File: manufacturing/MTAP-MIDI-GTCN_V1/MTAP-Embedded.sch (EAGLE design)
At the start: 15 parts, among them IC1 ESP32-WROOM-32D, IC2 AMS1117-3.3, X1 USB4140-GF-0230-C

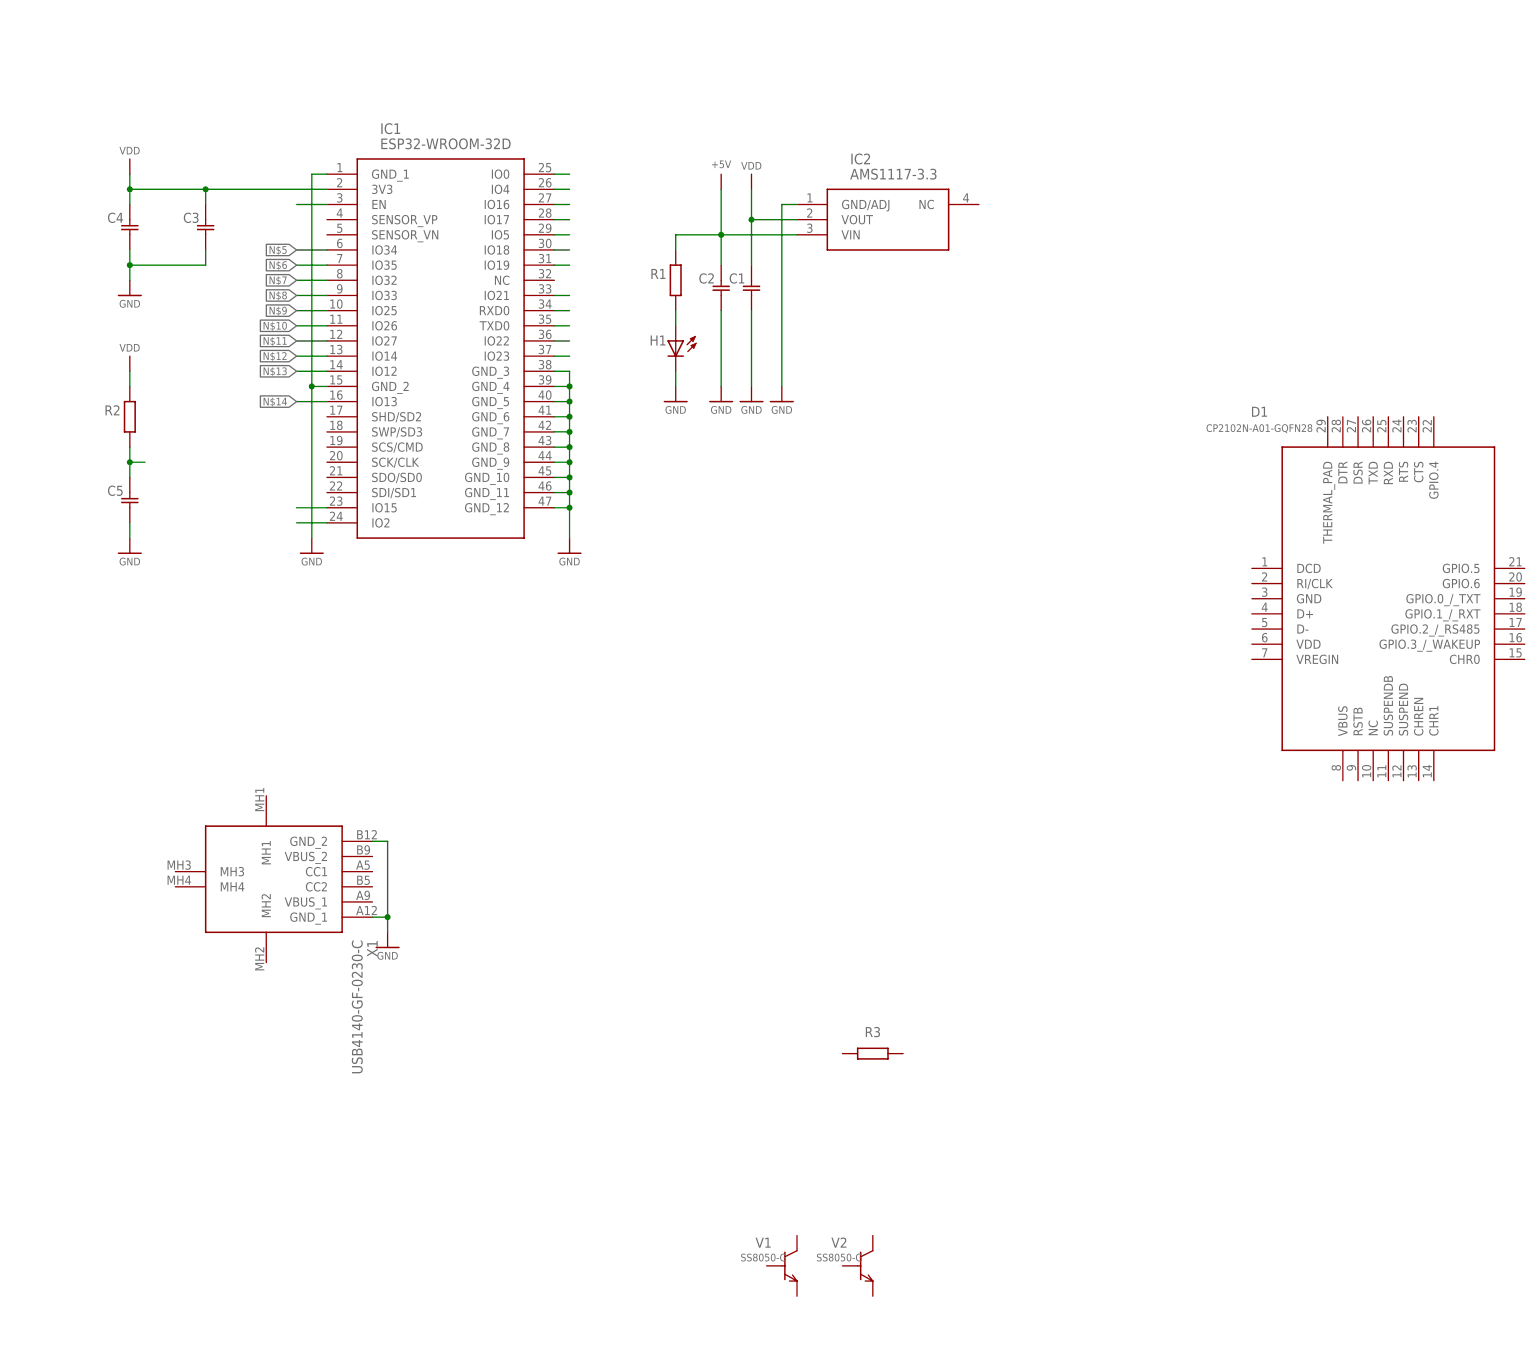
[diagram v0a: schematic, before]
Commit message: added Logo and tested ESP footprints
schematic for ESP complete
except values
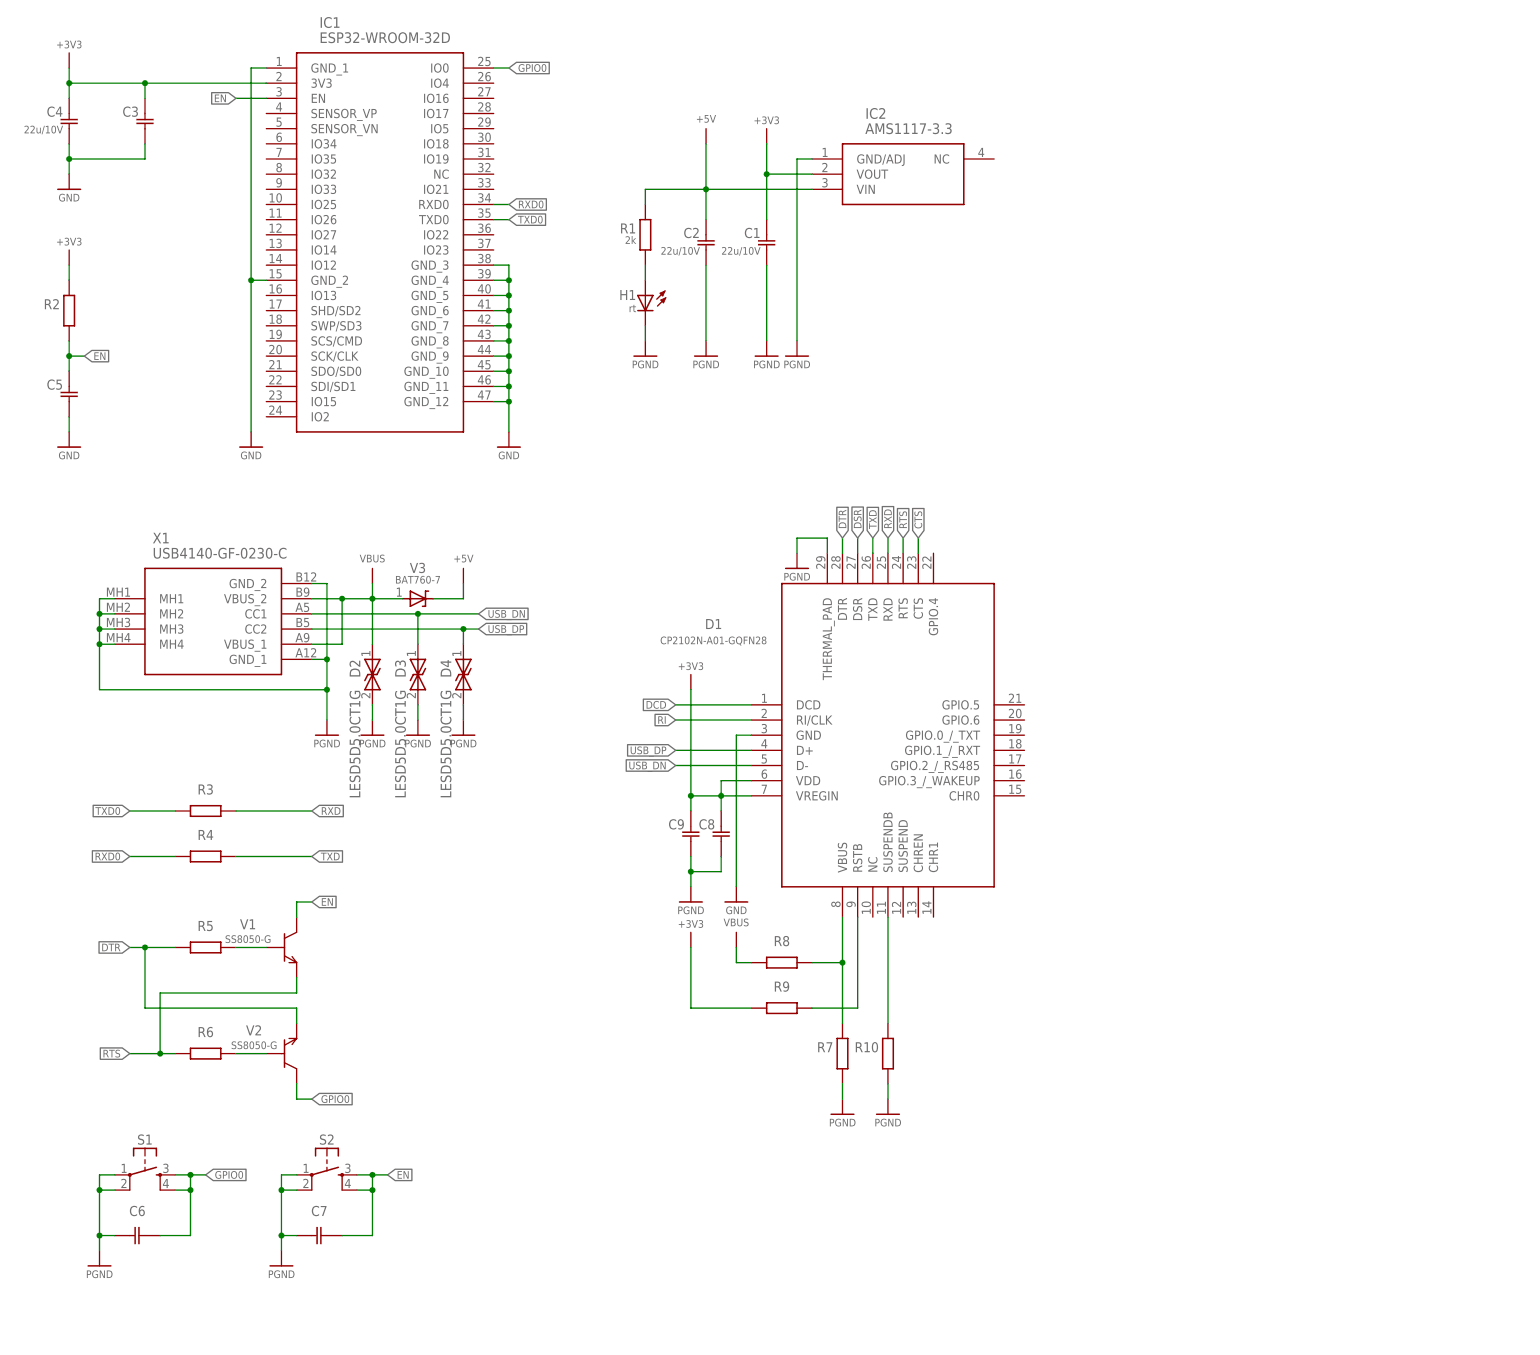
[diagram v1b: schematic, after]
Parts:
- added C6, C7: (no value), rcl_GruS:C-EULC0805
- added C8, C9: (no value), rcl_GruS:C-EUC0805
- added D2, D3, D4: LESD5D5.0CT1G, diode_GruS:LESD5D5.0CT1G
- added R10, R7: (no value), rcl_GruS:R-EUSR0805
- added R4, R5, R6, R8, R9: (no value), rcl_GruS:R-EU_R0805
- added S1, S2: (no value), switch_GruS:TASTE10XXSMD
- added V3: BAT760-7, diode_GruS:BAT760-7
- C1, C2, C4: value (none) -> 22u/10V
- H1: value (none) -> rt
- R1: value (none) -> 2k
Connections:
- removed net N$10: IC1.IO26
- removed net N$11: IC1.IO27
- removed net N$12: IC1.IO14
- removed net N$13: IC1.IO12
- removed net N$14: IC1.IO13
- removed net N$21: IC1.IO15
- removed net N$22: IC1.IO2
- removed net N$23: IC1.IO0
- removed net N$24: IC1.IO4
- removed net N$25: IC1.IO16
- removed net N$26: IC1.IO17
- removed net N$27: IC1.IO5
- removed net N$28: IC1.IO18
- removed net N$29: IC1.IO19
- removed net N$30: IC1.IO21
- removed net N$31: IC1.RXD0
- removed net N$32: IC1.TXD0
- removed net N$33: IC1.IO22
- removed net N$34: IC1.IO23
- removed net N$35: C5.1, R2.1
- removed net N$5: IC1.IO34
- removed net N$6: IC1.IO35
- removed net N$7: IC1.IO32
- removed net N$8: IC1.IO33
- removed net N$9: IC1.IO25
- removed net VDD: C1.1, C3.1, C4.1, IC1.3V3, IC2.VOUT, R2.2
- new net +3V3: C1.1, C3.1, C4.1, C8.1, C9.1, D1.VDD, D1.VREGIN, IC1.3V3, IC2.VOUT, R2.2, R9.1
- new net CTS: D1.CTS
- new net DCD: D1.DCD
- new net DSR: D1.DSR
- new net DTR: D1.DTR, R5.1, V2.E
- new net EN: C5.1, C7.1, IC1.EN, R2.1, S2.S, S2.S1, V1.C
- new net GPIO0: C6.1, IC1.IO0, S1.S, S1.S1, V2.C
- new net N$15: R5.2, V1.B
- new net N$16: R6.2, V2.B
- new net N$3: D1.SUSPENDB, R10.2
- new net N$4: D1.RSTB, R9.2
- new net PGND: C1.2, C2.2, C6.2, C7.2, C8.2, C9.2, D1.THERMAL_PAD, D2.2, D3.2, D4.2, H1.C, IC2.GND/ADJ, R10.1, R7.1, S1.P, S1.P1, S2.P, S2.P1, X1.GND_1, X1.GND_2, X1.MH1, X1.MH2, X1.MH3, X1.MH4
- new net RI: D1.RI/CLK
- new net RTS: D1.RTS, R6.1, V1.E
- new net RXD: D1.RXD, R3.2
- new net RXD0: IC1.RXD0, R4.1
- new net TXD: D1.TXD, R4.2
- new net TXD0: IC1.TXD0, R3.1
- new net USB_DN: D1.D-, D3.1, X1.CC1
- new net USB_DP: D1.D+, D4.1, X1.CC2
- new net VBUS: D2.1, R8.1, V3.K, X1.VBUS_1, X1.VBUS_2
- net +5V: now also V3.A
- net GND: now also D1.GND; no longer C1.2, C2.2, H1.C, IC2.GND/ADJ, X1.GND_1, X1.GND_2
- net N$2: now also D1.VBUS, R7.2, R8.2; no longer IC1.EN
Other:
- moved on the sheet: C1, C2, C3, C4, C5, D1, H1, IC1, IC2, R1, R2, R3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

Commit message: upd Embedded
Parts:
- added R11: 0R, rcl_GruS:R-EU_R0805
- IC1: value ESP32-WROOM-32D -> ESP32-WROOM-32UE-N8; device modul_GruS:ESP32-WROOM-32D -> modul_GruS:ESP32-WROOM-32UE-N8
- R7: value (none) -> 47k5
- R8: value (none) -> 22k1
- S1, S2: device switch_GruS:TASTE10XXSMD -> switch_GruS:TASTE10XXWE
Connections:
- net GND: now also R11.2
- net PGND: now also R11.1
- net USB_DN: now also D4.1, X1.CC2; no longer D3.1, X1.CC1
- net USB_DP: now also D3.1, X1.CC1; no longer D4.1, X1.CC2
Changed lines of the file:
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@@
 </variantdefs>
 <classes>
-<class number="0" name="default" width="0" drill="0">
+<class number="0" name="default" width="0.254" drill="0">
+</class>
+<class number="1" name="+3V3" width="0.8128" drill="0">
+</class>
+<class number="2" name="VBUS" width="0.8128" drill="0">
+</class>
+<class number="3" name="+5V" width="0.8128" drill="0">
 </class>
 </classes>
 <parts>
 <part name="FRAMES1" library="frames_GruS" library_urn="urn:adsk.eagle:library:27468648" deviceset="HTL-A4H-V1" device=""/>
-<part name="IC1" library="modul_GruS" library_urn="urn:adsk.eagle:library:13580331" deviceset="ESP32-WROOM-32D" device="" package3d_urn="urn:adsk.eagle:package:37740908/1"/>
+<part name="IC1" library="modul_GruS" library_urn="urn:adsk.eagle:library:13580331" deviceset="ESP32-WROOM-32UE-N8" device="" package3d_urn="urn:adsk.eagle:package:37940893/1"/>
 <part name="IC2" library="vreg_GruS" library_urn="urn:adsk.eagle:library:13581047" deviceset="AMS1117-3.3" device="" package3d_urn="urn:adsk.eagle:package:37738375/1"/>
 <part name="C1" library="rcl_GruS" library_urn="urn:adsk.eagle:library:13572313" deviceset="C-EU" device="C0805" package3d_urn="urn:adsk.eagle:package:23617/2" value="22u/10V"/>
@@
 <part name="V2" library="transistor_GruS" library_urn="urn:adsk.eagle:library:13581291" deviceset="SS8050-G" device="" package3d_urn="urn:adsk.eagle:package:37738390/1"/>
 <part name="D1" library="ic_GruS" library_urn="urn:adsk.eagle:library:13571010" deviceset="CP2102N-A01-GQFN28" device="" package3d_urn="urn:adsk.eagle:package:37738757/2"/>
-<part name="X1" library="con_GruS" library_urn="urn:adsk.eagle:library:13569504" deviceset="USB4140-GF-0230-C" device="" package3d_urn="urn:adsk.eagle:package:37738890/1"/>
+<part name="X1" library="con_GruS" library_urn="urn:adsk.eagle:library:13569504" deviceset="USB4140-GF-0230-C" device="" package3d_urn="urn:adsk.eagle:package:37738890/2"/>
 <part name="D2" library="diode_GruS" library_urn="urn:adsk.eagle:library:13569696" deviceset="LESD5D5.0CT1G" device="" package3d_urn="urn:adsk.eagle:package:37738879/1"/>
 <part name="D3" library="diode_GruS" library_urn="urn:adsk.eagle:library:13569696" deviceset="LESD5D5.0CT1G" device="" package3d_urn="urn:adsk.eagle:package:37738879/1"/>
@@
 <part name="R6" library="rcl_GruS" library_urn="urn:adsk.eagle:library:13572313" deviceset="R-EU_" device="R0805" package3d_urn="urn:adsk.eagle:package:18365371/1"/>
 <part name="VBUS1" library="supply_GruS" library_urn="urn:adsk.eagle:library:13579815" deviceset="VBUS" device=""/>
-<part name="S1" library="switch_GruS" library_urn="urn:adsk.eagle:library:13571161" deviceset="TASTE10XX" device="SMD" package3d_urn="urn:adsk.eagle:package:18368075/2"/>
+<part name="S1" library="switch_GruS" library_urn="urn:adsk.eagle:library:13571161" deviceset="TASTE10XX" device="WE" package3d_urn="urn:adsk.eagle:package:18368072/1"/>
 <part name="C6" library="rcl_GruS" library_urn="urn:adsk.eagle:library:13572313" deviceset="C-EUL" device="C0805" package3d_urn="urn:adsk.eagle:package:23617/2"/>
-<part name="S2" library="switch_GruS" library_urn="urn:adsk.eagle:library:13571161" deviceset="TASTE10XX" device="SMD" package3d_urn="urn:adsk.eagle:package:18368075/2"/>
+<part name="S2" library="switch_GruS" library_urn="urn:adsk.eagle:library:13571161" deviceset="TASTE10XX" device="WE" package3d_urn="urn:adsk.eagle:package:18368072/1"/>
 <part name="C7" library="rcl_GruS" library_urn="urn:adsk.eagle:library:13572313" deviceset="C-EUL" device="C0805" package3d_urn="urn:adsk.eagle:package:23617/2"/>
 <part name="+3V1" library="supply_GruS" library_urn="urn:adsk.eagle:library:13579815" deviceset="+3V3" device=""/>
@@
 <part name="R9" library="rcl_GruS" library_urn="urn:adsk.eagle:library:13572313" deviceset="R-EU_" device="R0805" package3d_urn="urn:adsk.eagle:package:18365371/1"/>
 <part name="+3V2" library="supply_GruS" library_urn="urn:adsk.eagle:library:13579815" deviceset="+3V3" device=""/>
-<part name="R7" library="rcl_GruS" library_urn="urn:adsk.eagle:library:13572313" deviceset="R-EUS" device="R0805" package3d_urn="urn:adsk.eagle:package:18365371/1"/>
-<part name="R8" library="rcl_GruS" library_urn="urn:adsk.eagle:library:13572313" deviceset="R-EU_" device="R0805" package3d_urn="urn:adsk.eagle:package:18365371/1"/>
+<part name="R7" library="rcl_GruS" library_urn="urn:adsk.eagle:library:13572313" deviceset="R-EUS" device="R0805" package3d_urn="urn:adsk.eagle:package:18365371/1" value="47k5"/>
+<part name="R8" library="rcl_GruS" library_urn="urn:adsk.eagle:library:13572313" deviceset="R-EU_" device="R0805" package3d_urn="urn:adsk.eagle:package:18365371/1" value="22k1"/>
 <part name="+3V3" library="supply_GruS" library_urn="urn:adsk.eagle:library:13579815" deviceset="+3V3" device=""/>
 <part name="+3V4" library="supply_GruS" library_urn="urn:adsk.eagle:library:13579815" deviceset="+3V3" device=""/>
@@
 <part name="PGND14" library="supply_GruS" library_urn="urn:adsk.eagle:library:13579815" deviceset="PGND" device=""/>
 <part name="PGND15" library="supply_GruS" library_urn="urn:adsk.eagle:library:13579815" deviceset="PGND" device=""/>
+<part name="R11" library="rcl_GruS" library_urn="urn:adsk.eagle:library:13572313" deviceset="R-EU_" device="R0805" package3d_urn="urn:adsk.eagle:package:18365371/1" value="0R"/>
+<part name="PGND13" library="supply_GruS" library_urn="urn:adsk.eagle:library:13579815" deviceset="PGND" device=""/>
+<part name="GND2" library="supply_GruS" library_urn="urn:adsk.eagle:library:13579815" deviceset="GND" device=""/>
 </parts>
 <sheets>
@@
 <instance part="PGND15" gate="G$1" x="142.24" y="83.82" smashed="yes">
 <attribute name="VALUE" x="142.24" y="81.788" size="1.27" layer="96" font="vector" align="bottom-center"/>
+</instance>
+<instance part="R11" gate="G$1" x="106.68" y="86.36" smashed="yes">
+<attribute name="NAME" x="106.68" y="89.1286" size="1.6764" layer="95" font="vector" align="bottom-center"/>
+<attribute name="VALUE" x="106.68" y="87.63" size="1.27" layer="96" font="vector" align="bottom-center"/>
+</instance>
+<instance part="PGND13" gate="G$1" x="99.06" y="81.28" smashed="yes">
+<attribute name="VALUE" x="99.06" y="79.248" size="1.27" layer="96" font="vector" align="bottom-center"/>
+</instance>
+<instance part="GND2" gate="1" x="114.3" y="81.28" smashed="yes">
+<attribute name="VALUE" x="114.3" y="79.248" size="1.27" layer="96" font="vector" align="bottom-center"/>
 </instance>
 </instances>
@@
 <pinref part="GND1" gate="1" pin="GND"/>
 </segment>
+<segment>
+<pinref part="R11" gate="G$1" pin="2"/>
+<wire x1="111.76" y1="86.36" x2="114.3" y2="86.36" width="0.1524" layer="91"/>
+<wire x1="114.3" y1="86.36" x2="114.3" y2="83.82" width="0.1524" layer="91"/>
+<pinref part="GND2" gate="1" pin="GND"/>
+</segment>
 </net>
 <net name="N$1" class="0">
@@
 <net name="USB_DP" class="0">
 <segment>
+<pinref part="D1" gate="G$1" pin="D+"/>
+<wire x1="127" y1="144.78" x2="114.3" y2="144.78" width="0.1524" layer="91"/>
+<label x="114.3" y="144.78" size="1.27" layer="95" rot="R180" xref="yes"/>
+</segment>
+<segment>
+<pinref part="X1" gate="G$1" pin="CC1"/>
+<wire x1="53.34" y1="167.64" x2="71.12" y2="167.64" width="0.1524" layer="91"/>
+<pinref part="D3" gate="G$1" pin="1"/>
+<wire x1="71.12" y1="167.64" x2="81.28" y2="167.64" width="0.1524" layer="91"/>
+<wire x1="71.12" y1="162.56" x2="71.12" y2="167.64" width="0.1524" layer="91"/>
+<junction x="71.12" y="167.64"/>
+<label x="81.28" y="167.64" size="1.27" layer="95" xref="yes"/>
+</segment>
+</net>
+<net name="USB_DN" class="0">
+<segment>
+<pinref part="D1" gate="G$1" pin="D-"/>
+<wire x1="127" y1="142.24" x2="114.3" y2="142.24" width="0.1524" layer="91"/>
+<label x="114.3" y="142.24" size="1.27" layer="95" rot="R180" xref="yes"/>
+</segment>
+<segment>
 <pinref part="X1" gate="G$1" pin="CC2"/>
 <wire x1="53.34" y1="165.1" x2="78.74" y2="165.1" width="0.1524" layer="91"/>
@@
 <wire x1="78.74" y1="162.56" x2="78.74" y2="165.1" width="0.1524" layer="91"/>
 <junction x="78.74" y="165.1"/>
-</segment>
-<segment>
-<pinref part="D1" gate="G$1" pin="D+"/>
-<wire x1="127" y1="144.78" x2="114.3" y2="144.78" width="0.1524" layer="91"/>
-<label x="114.3" y="144.78" size="1.27" layer="95" rot="R180" xref="yes"/>
-</segment>
-</net>
-<net name="USB_DN" class="0">
-<segment>
-<pinref part="X1" gate="G$1" pin="CC1"/>
-<wire x1="53.34" y1="167.64" x2="71.12" y2="167.64" width="0.1524" layer="91"/>
-<pinref part="D3" gate="G$1" pin="1"/>
-<wire x1="71.12" y1="167.64" x2="81.28" y2="167.64" width="0.1524" layer="91"/>
-<wire x1="71.12" y1="162.56" x2="71.12" y2="167.64" width="0.1524" layer="91"/>
-<junction x="71.12" y="167.64"/>
-<label x="81.28" y="167.64" size="1.27" layer="95" xref="yes"/>
-</segment>
-<segment>
-<pinref part="D1" gate="G$1" pin="D-"/>
-<wire x1="127" y1="142.24" x2="114.3" y2="142.24" width="0.1524" layer="91"/>
-<label x="114.3" y="142.24" size="1.27" layer="95" rot="R180" xref="yes"/>
 </segment>
 </net>
@@
 <pinref part="R7" gate="G$1" pin="1"/>
 </segment>
-</net>
+<segment>
+<pinref part="R11" gate="G$1" pin="1"/>
+<wire x1="101.6" y1="86.36" x2="99.06" y2="86.36" width="0.1524" layer="91"/>
+<wire x1="99.06" y1="86.36" x2="99.06" y2="83.82" width="0.1524" layer="91"/>
+<pinref part="PGND13" gate="G$1" pin="PGND"/>
+</segment>
+</net>

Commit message: Update Embedded
added PCM ADC to PCB
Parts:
- added C10, C12: 1u, rcl_GruS:C-EUC0805
- added C11, C13, C14: 10u, rcl_GruS:C-EUC0805
- added C15, C17, C18, C20: 100n, rcl_GruS:C-EUC0805
- added IC3: PCM1821IRTER, adc-dac_GruS:PCM1821IRTER
- added X2: (no value), con_GruS:JUMPSMD1FACH-1SHORT
- C3, C5: value (none) -> 100n/50V
- C6, C7: value (none) -> 100n
- R10, R2, R5, R6: value (none) -> 10k
- R11: device rcl_GruS:R-EU_R0805 -> con_GruS:JUMPSMD1FACH-1SHORT
- R3, R4: value (none) -> 0R
- R9: value (none) -> 2k
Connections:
- new net AVDD: C12.1, C18.1, IC3.AVDD, X2.2
- new net BCLK: IC1.IO22, IC3.BCLK
- new net FSYNC: IC1.IO23, IC3.FSYNC
- new net FTM0: IC3.FMT0
- new net GPIO12: IC1.IO12
- new net GPIO13: IC1.IO13
- new net GPIO14: IC1.IO14
- new net GPIO15: IC1.IO15
- new net GPIO16: IC1.IO16
- new net GPIO17: IC1.IO17
- new net GPIO2: IC1.IO2
- new net GPIO25: IC1.IO25
- new net GPIO26: IC1.IO26
- new net GPIO27: IC1.IO27
- new net GPIO32: IC1.IO32
- new net GPIO33: IC1.IO33
- new net GPIO34: IC1.IO34
- new net GPIO35: IC1.IO35
- new net GPIO4: IC1.IO4
- new net IN1M: IC3.IN1M
- new net IN1P: IC3.IN1P
- new net IN2M: IC3.IN2M
- new net IN2P: IC3.IN2P
- new net MD0: IC1.IO18, IC3.MD0
- new net MD1: IC1.IO19, IC3.MD1
- new net MSZ: IC1.IO5, IC3.MSZ
- new net N$13: C11.1, C15.1, IC3.DREG
- new net N$17: C13.1, C17.1, IC3.AREG
- new net N$9: C10.1, IC3.VREF
- new net SDATA: IC1.IO21, IC3.SDOUT
- net +3V3: now also C14.1, C20.1, IC3.IOVDD, X2.1
- net GND: now also C10.2, C11.2, C12.2, C13.2, C14.2, C15.2, C17.2, C18.2, C20.2, IC3.VSS_1, IC3.VSS_2, IC3.VSS_3, IC3.VSS_4, IC3.VSS_5, IC3.VSS_6, IC3.VSS_7, IC3.VSS_8, IC3.VSS_9
